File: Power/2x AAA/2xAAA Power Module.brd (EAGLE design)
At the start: 25.4 x 25.4 mm, 3 parts

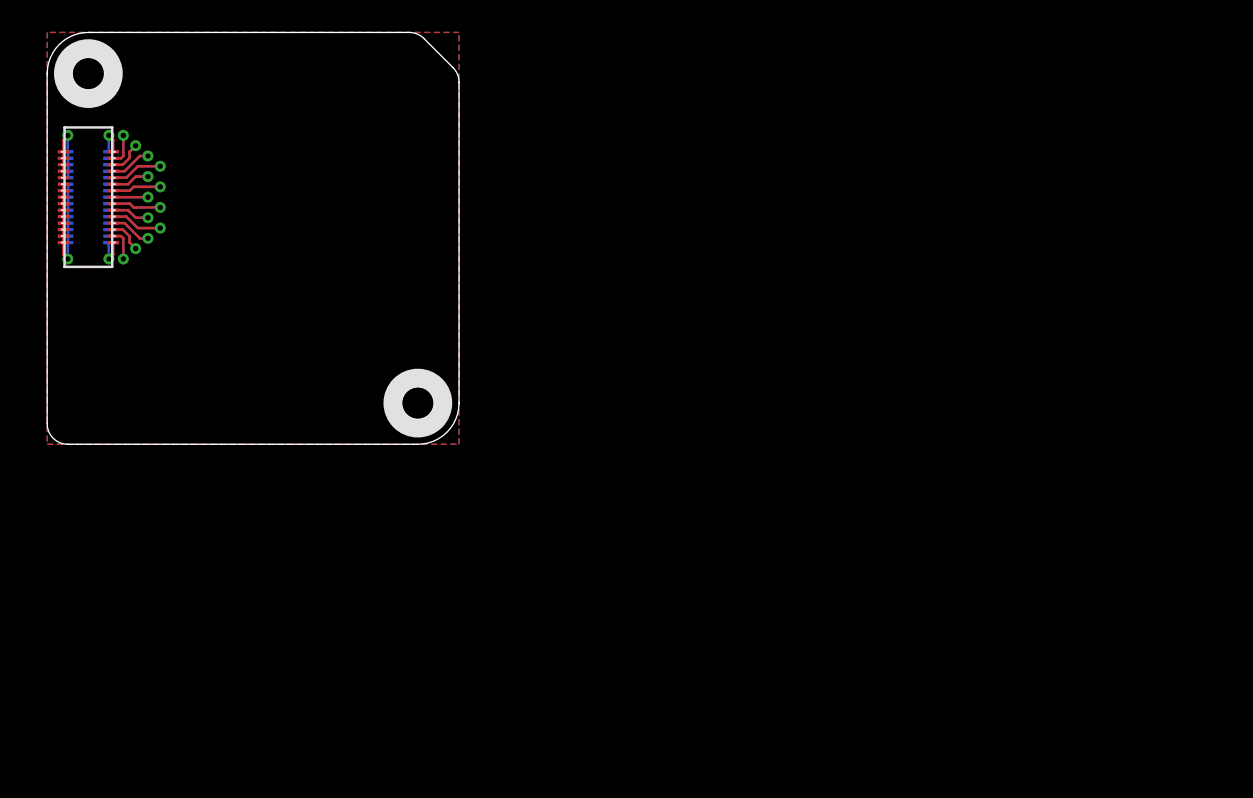
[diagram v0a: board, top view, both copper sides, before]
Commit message: Trying out different connectors
Signed-off-by: Cruz Monrreal II <Cruz.Monrreal@gmail.com>
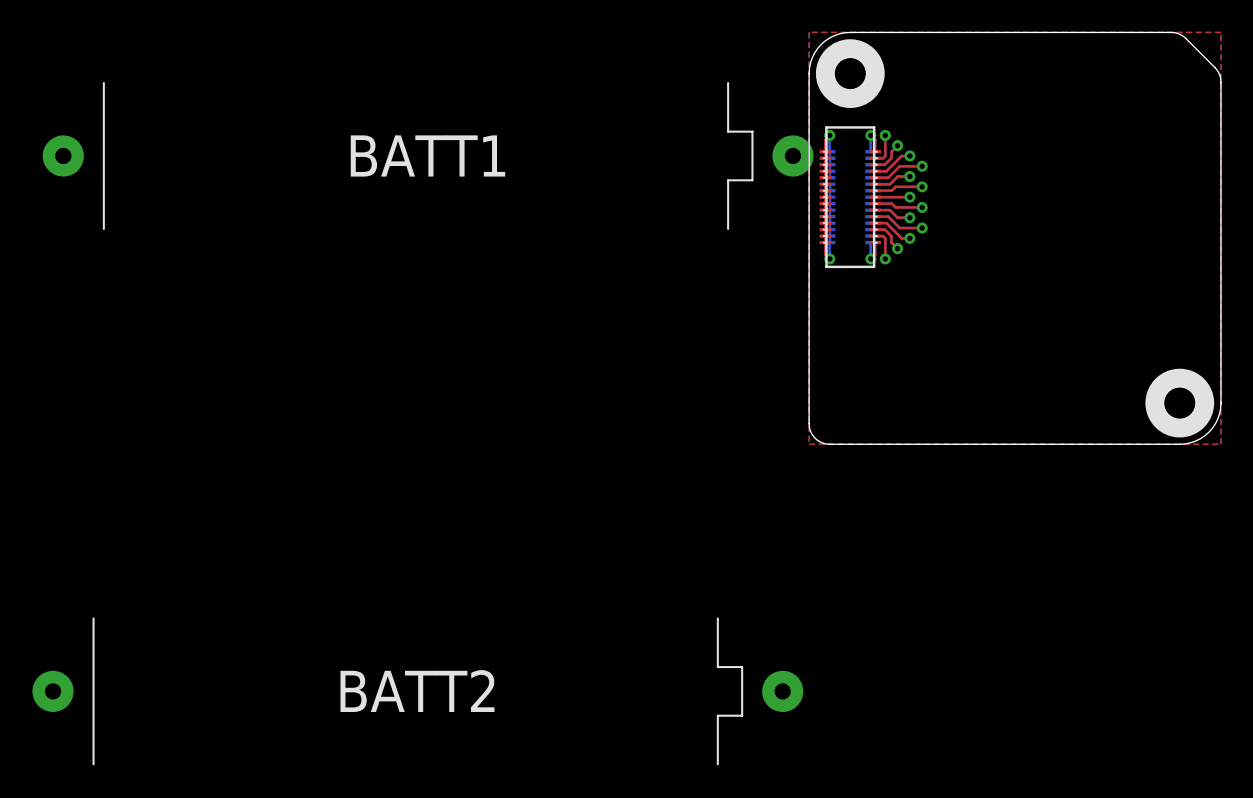
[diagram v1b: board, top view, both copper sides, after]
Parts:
- added BATT1, BATT2: AAA, adafruit:12BH412
- moved U$4 47.0 mm to (49.5, 22.9)
- moved U$8 47.0 mm to (47.0, 0.00)
- moved U$3 47.0 mm to (69.8, 2.54)
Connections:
- new net N$16: BATT1.-, BATT2.+
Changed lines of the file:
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@@
 <board>
 <plain>
-<wire x1="0" y1="22.86" x2="0" y2="1.27" width="0" layer="20"/>
-<wire x1="0" y1="1.27" x2="1.27" y2="0" width="0" layer="20" curve="90"/>
-<wire x1="1.27" y1="0" x2="22.86" y2="0" width="0" layer="20"/>
-<wire x1="22.86" y1="0" x2="25.4" y2="2.54" width="0" layer="20" curve="90"/>
-<wire x1="25.4" y1="2.54" x2="25.4" y2="22.33395" width="0" layer="20"/>
-<wire x1="25.4" y1="22.33395" x2="25.028025" y2="23.231975" width="0" layer="20" curve="45"/>
-<wire x1="25.028025" y1="23.231975" x2="23.231975" y2="25.028025" width="0" layer="20"/>
-<wire x1="23.231975" y1="25.028025" x2="22.33395" y2="25.4" width="0" layer="20" curve="45"/>
-<wire x1="22.33395" y1="25.4" x2="2.54" y2="25.4" width="0" layer="20"/>
-<wire x1="2.54" y1="25.4" x2="0" y2="22.86" width="0" layer="20" curve="90"/>
+<wire x1="46.99" y1="22.86" x2="46.99" y2="1.27" width="0" layer="20"/>
+<wire x1="46.99" y1="1.27" x2="48.26" y2="0" width="0" layer="20" curve="90"/>
+<wire x1="48.26" y1="0" x2="69.85" y2="0" width="0" layer="20"/>
+<wire x1="69.85" y1="0" x2="72.39" y2="2.54" width="0" layer="20" curve="90"/>
+<wire x1="72.39" y1="2.54" x2="72.39" y2="22.33395" width="0" layer="20"/>
+<wire x1="72.39" y1="22.33395" x2="72.018025" y2="23.231975" width="0" layer="20" curve="45"/>
+<wire x1="72.018025" y1="23.231975" x2="70.221975" y2="25.028025" width="0" layer="20"/>
+<wire x1="70.221975" y1="25.028025" x2="69.32395" y2="25.4" width="0" layer="20" curve="45"/>
+<wire x1="69.32395" y1="25.4" x2="49.53" y2="25.4" width="0" layer="20"/>
+<wire x1="49.53" y1="25.4" x2="46.99" y2="22.86" width="0" layer="20" curve="90"/>
 </plain>
 <attributes>
@@
 </autorouter>
 <elements>
-<element name="U$4" library=".screw_holes" package="2MM" value="HOLE.2MM" x="2.54" y="22.86" rot="R90"/>
-<element name="U$3" library=".screw_holes" package="2MM" value="HOLE.2MM" x="22.86" y="2.54" rot="R90"/>
-<element name="U$8" library="thinkmaketest" package="ROOT1.BOTH" value="ROOT1.BOTH" x="0" y="0"/>
+<element name="U$4" library=".screw_holes" package="2MM" value="HOLE.2MM" x="49.53" y="22.86" rot="R90"/>
+<element name="U$3" library=".screw_holes" package="2MM" value="HOLE.2MM" x="69.85" y="2.54" rot="R90"/>
+<element name="U$8" library="thinkmaketest" package="ROOT1.BOTH" value="ROOT1.BOTH" x="46.99" y="0"/>
+<element name="BATT1" library="adafruit" package="12BH412" value="AAA" x="23.495" y="17.78"/>
+<element name="BATT2" library="adafruit" package="12BH412" value="AAA" x="22.86" y="-15.24"/>
 </elements>
 <signals>
 <signal name="GND">
 <polygon width="0.2032" layer="16">
-<vertex x="0" y="0"/>
-<vertex x="25.4" y="0"/>
-<vertex x="25.4" y="25.4"/>
-<vertex x="0" y="25.4"/>
+<vertex x="46.99" y="0"/>
+<vertex x="72.39" y="0"/>
+<vertex x="72.39" y="25.4"/>
+<vertex x="46.99" y="25.4"/>
 </polygon>
 <polygon width="0.2032" layer="1">
-<vertex x="0" y="0"/>
-<vertex x="25.4" y="0"/>
-<vertex x="25.4" y="25.4"/>
-<vertex x="0" y="25.4"/>
+<vertex x="46.99" y="0"/>
+<vertex x="72.39" y="0"/>
+<vertex x="72.39" y="25.4"/>
+<vertex x="46.99" y="25.4"/>
 </polygon>
 <contactref element="U$8" pad="GND@17"/>
@@
 <contactref element="U$8" pad="WAKE"/>
 </signal>
+<signal name="N$16">
+<contactref element="BATT2" pad="+"/>
+<contactref element="BATT1" pad="-"/>
+<wire x1="0.995" y1="17.78" x2="45.36" y2="-15.24" width="0" layer="19" extent="1-1"/>
+</signal>
 </signals>

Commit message: Added note as to which connectors to use
Signed-off-by: Cruz Monrreal II <Cruz.Monrreal@gmail.com>
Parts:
- removed BATT1, BATT2: AAA, adafruit:12BH412
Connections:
- removed net N$16: BATT1.-, BATT2.+
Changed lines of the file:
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@@
 <element name="U$3" library=".screw_holes" package="2MM" value="HOLE.2MM" x="69.85" y="2.54" rot="R90"/>
 <element name="U$8" library="thinkmaketest" package="ROOT1.BOTH" value="ROOT1.BOTH" x="46.99" y="0"/>
-<element name="BATT1" library="adafruit" package="12BH412" value="AAA" x="23.495" y="17.78"/>
-<element name="BATT2" library="adafruit" package="12BH412" value="AAA" x="22.86" y="-15.24"/>
 </elements>
 <signals>
@@
 <contactref element="U$8" pad="WAKE"/>
 </signal>
-<signal name="N$16">
-<contactref element="BATT2" pad="+"/>
-<contactref element="BATT1" pad="-"/>
-<wire x1="0.995" y1="17.78" x2="45.36" y2="-15.24" width="0" layer="19" extent="1-1"/>
-</signal>
 </signals>
